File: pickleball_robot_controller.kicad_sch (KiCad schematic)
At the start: 74 parts, among them J1 BATTERY_XT60_PIGTAIL, J10 PI_UART_CONTROL, J11 SERVO_6V_10A_INPUT, J12 MAIN_SWING_25KG_SERVO, J13 ELBOW_MG996R_SERVO, J14 WRIST_MG90S_SERVO, J2 ESP32_PICO_KIT_V4.1_CARRIER, J4 LEFT_MOTOR, J5 RIGHT_MOTOR, J6 LEFT_ENCODER, J7 RIGHT_ENCODER, J8 PI_5V_5A_INPUT, J9 PI_POWER_OUT_2x5V_2xGND, U1 LM2596S-5.0, U2 VNH5019A-E, U3 VNH5019A-E, U5 PCA9685PW, U6 74LVC1G14, U7 74LVC1G14, U8 74LVC1G14, U9 74LVC1G14

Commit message: Improve schematic readability and add power guidance
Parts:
- added D5: GREEN: ESP32/LOGIC, LED_SMD:LED_0805_2012Metric, symbol Device:LED
- added D6: BLUE: PI 5V, LED_SMD:LED_0805_2012Metric, symbol Device:LED
- added D7: AMBER: SERVO 6V, LED_SMD:LED_0805_2012Metric, symbol Device:LED
- added D8: RED: MOTOR FAULT, LED_SMD:LED_0805_2012Metric, symbol Device:LED
- added R100: 1k CTRL POWER, Resistor_SMD:R_0805_2012Metric, symbol Device:R
- added R101: 1k PI POWER, Resistor_SMD:R_0805_2012Metric, symbol Device:R
- added R102: 1k SERVO POWER, Resistor_SMD:R_0805_2012Metric, symbol Device:R
- added R103: 1k FAULT LED, Resistor_SMD:R_0805_2012Metric, symbol Device:R
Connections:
- net +5V_CTRL: now also R100.2
- net 3V3: now also R103.2
- net GND: now also D5.1 (K), D6.1 (K), D7.1 (K)
- net MOTOR_DIAG: now also D8.1 (K)
- net PI_5V: now also R101.2
- net SERVO_6V: now also R102.2
- new net LED_CTRL_PWR: D5.2 (A), R100.1
- new net LED_FAULT_ANODE: D8.2 (A), R103.1
- new net LED_PI_PWR: D6.2 (A), R101.1
- new net LED_SERVO_PWR: D7.2 (A), R102.1
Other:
- note added: "Green = ESP32 logic alive; blue = Pi 5V present; amber = servo 6V present; red = motor driver fault."
- note added: "One 3S battery is used. Separate regulators create PI_5V, +5V_CTRL, and SERVO_6V."
- note added: "STATUS LEDs"
- note added: "Servo 1 = main swing; Servo 2 = elbow; Servo 3 = wrist. Pin order: GND / regulated 6V / PWM."
- note removed: "Servo pin order: 1 GND, 2 regulated 6V, 3 PWM. Verify cable colors before plugging in."

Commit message: Add Pi 5V buck design and clean schematic layout
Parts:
- removed J8: PI_5V_5A_INPUT, TerminalBlock:TerminalBlock_MaiXu_MX126-5.0-02P_1x02_P5.00mm, symbol Connector_Generic:Conn_01x02
- added C31: 100nF BOOT, Capacitor_SMD:C_0805_2012Metric, symbol Device:C
- added C32, C33, C34, C35: 2.2uF 25V X7R, Capacitor_SMD:C_1206_3216Metric, symbol Device:C
- added C36: 4.7nF COMP, Capacitor_SMD:C_0805_2012Metric, symbol Device:C
- added C37: 47pF COMP, Capacitor_SMD:C_0805_2012Metric, symbol Device:C
- added C38, C39, C44: 47uF 10V X7R, Capacitor_SMD:C_1210_3225Metric, symbol Device:C
- added D9: B560C 5A, Diode_SMD:D_SMC, symbol Device:D_Schottky
- added F3: 5A PI OUTPUT FUSE, Fuse:Fuse_1206_3216Metric, symbol Device:Fuse
- added L2: 7.2uH >=8A SHIELDED, Inductor_SMD:L_1210_3225Metric, symbol Device:L
- added R30: 243k RT SET, Resistor_SMD:R_0805_2012Metric, symbol Device:R
- added R31: 442k FB TOP 1%, Resistor_SMD:R_0805_2012Metric, symbol Device:R
- added R32: 90.9k FB BOTTOM 1%, Resistor_SMD:R_0805_2012Metric, symbol Device:R
- added R33: 10.2k COMP, Resistor_SMD:R_0805_2012Metric, symbol Device:R
- added U4: TPS54560BDDA — 5V / 5A, Package_SO:TI_SO-PowerPAD-8_ThermalVias, symbol Regulator_Switching:TPS54560BDDA
- C30: value 1000uF 10V LOW_ESR -> 1000uF 10V LOW ESR
- D5: value GREEN: ESP32/LOGIC -> GREEN
- D6: value BLUE: PI 5V -> BLUE
- D7: value AMBER: SERVO 6V -> AMBER
- D8: value RED: MOTOR FAULT -> RED
- J9: value PI_POWER_OUT_2x5V_2xGND -> PI POWER: 2x5V + 2xGND
- R100: value 1k CTRL POWER -> 1k
- R101: value 1k PI POWER -> 1k
- R102: value 1k SERVO POWER -> 1k
- R103: value 1k FAULT LED -> 1k
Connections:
- net +5V_CTRL: now also R100.1; no longer R100.2
- net 3V3: now also R103.1; no longer R103.2
- net GND: now also D5.2 (A), D6.2 (A), D7.2 (A), C32.2, C33.2, C34.2, C35.2, C36.2, C37.2, C38.2, C39.2, C44.2, D9.1 (K), R30.2, R32.2, U4.7 (GND), U4.9 (GND); no longer D5.1 (K), D6.1 (K), D7.1 (K)
- net LED_CTRL_PWR: now also D5.1 (K), R100.2; no longer D5.2 (A), R100.1
- net LED_FAULT_ANODE: now also D8.1 (K), R103.2; no longer D8.2 (A), R103.1
- net LED_PI_PWR: now also D6.1 (K), R101.2; no longer D6.2 (A), R101.1
- net LED_SERVO_PWR: now also D7.1 (K), R102.2; no longer D7.2 (A), R102.1
- net MOTOR_DIAG: now also D8.2 (A); no longer D8.1 (K)
- net PI_5V: now also R101.1, F3.2; no longer R101.2
- net SERVO_6V: now also R102.1; no longer R102.2
- net VBAT_SW: now also C32.1, C33.1, C34.1, C35.1, U4.2 (VIN), U4.3 (EN)
- new net PI_5V_RAW: C38.1, C39.1, C44.1, F3.1, L2.2, R31.1
- new net PI_BOOT: C31.1, U4.1 (BOOT)
- new net PI_BUCK_SW: C31.2, D9.2 (A), L2.1, U4.8 (SW)
- new net PI_COMP: C37.1, R33.1, U4.6 (COMP)
- new net PI_COMP_RC: C36.1, R33.2
- new net PI_FB: R31.2, R32.1, U4.5 (FB)
- new net PI_RT: R30.1, U4.4 (RT/CLK)
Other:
- note added: "D5 GREEN: control 5V D6 BLUE: Pi 5V D7 AMBER: servo 6V D8 RED: motor driver fault"
- note added: "ESP32-PICO-KIT carrier uses the confirmed 17.78mm row spacing."
- note added: "RASPBERRY PI 5V / 5A BUCK — TPS54560B"
- note added: "U4 values are the TI 12V-to-5V / 5A reference design. Follow TI layout guidance; do not use this rail for motors or servos."
- note added: "Use Mini-Fit Jr / screw terminal, not 0.1in headers, for Pi power. Keep this 5A path short and wide."
- note removed: "DIP-34 W17.78mm is a provisional carrier pad pattern; verify against the real board before ordering."
- note removed: "Green = ESP32 logic alive; blue = Pi 5V present; amber = servo 6V present; red = motor driver fault."
- note removed: "One 3S battery is used. Separate regulators create PI_5V, +5V_CTRL, and SERVO_6V."
- note removed: "RASPBERRY PI 5 POWER PASS-THROUGH (SEPARATE 5V/5A REGULATOR)"
- note removed: "Use Mini-Fit Jr / screw terminal, not ordinary 0.1in headers, for Pi 5 A power."

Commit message: Right-size servo power and add motor cable connectors
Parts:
- removed J4: LEFT_MOTOR, TerminalBlock:TerminalBlock_MaiXu_MX126-5.0-02P_1x02_P5.00mm, symbol Connector_Generic:Conn_01x02
- removed J5: RIGHT_MOTOR, TerminalBlock:TerminalBlock_MaiXu_MX126-5.0-02P_1x02_P5.00mm, symbol Connector_Generic:Conn_01x02
- removed J6: LEFT_ENCODER, Connector_JST:JST_XH_B4B-XH-A_1x04_P2.50mm_Vertical, symbol Connector_Generic:Conn_01x04
- removed J7: RIGHT_ENCODER, Connector_JST:JST_XH_B4B-XH-A_1x04_P2.50mm_Vertical, symbol Connector_Generic:Conn_01x04
- added C45: 100nF BOOT, Capacitor_SMD:C_0805_2012Metric, symbol Device:C
- added C46, C47: 2.2uF 25V X7R, Capacitor_SMD:C_1206_3216Metric, symbol Device:C
- added C48: 4.7nF COMP, Capacitor_SMD:C_0805_2012Metric, symbol Device:C
- added C49: 47pF COMP, Capacitor_SMD:C_0805_2012Metric, symbol Device:C
- added C50, C51: 47uF 10V X7R, Capacitor_SMD:C_1210_3225Metric, symbol Device:C
- added D10: B560C 5A, Diode_SMD:D_SMC, symbol Device:D_Schottky
- added J4: LEFT_GA25_370_MOTOR_ENCODER, Connector_JST:JST_GH_BM06B-GHS-TBT_1x06-1MP_P1.25mm_Vertical, symbol Connector_Generic:Conn_01x06
- added J5: RIGHT_GA25_370_MOTOR_ENCODER, Connector_JST:JST_GH_BM06B-GHS-TBT_1x06-1MP_P1.25mm_Vertical, symbol Connector_Generic:Conn_01x06
- added L3: 6.8uH >=8A SHIELDED, Inductor_SMD:L_1210_3225Metric, symbol Device:L
- added R104: 243k RT SET, Resistor_SMD:R_0805_2012Metric, symbol Device:R
- added R105: 590k FB TOP 1%, Resistor_SMD:R_0805_2012Metric, symbol Device:R
- added R106: 90.9k FB BOTTOM 1%, Resistor_SMD:R_0805_2012Metric, symbol Device:R
- added R107: 10.2k COMP, Resistor_SMD:R_0805_2012Metric, symbol Device:R
- added U10: TPS54560BDDA — 6V / 5A, Package_SO:TI_SO-PowerPAD-8_ThermalVias, symbol Regulator_Switching:TPS54560BDDA
- F2: value 15A_EXTERNAL_SERVO_FUSE -> 7.5A_SERVO_OUTPUT_FUSE
- J11: value SERVO_6V_10A_INPUT -> SERVO_6V_POWER_OUT
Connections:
- net 3V3: now also J4.4 (Pin_4), J5.4 (Pin_4)
- net GND: now also C46.2, C47.2, C48.2, C49.2, C50.2, C51.2, D10.1 (K), J4.3 (Pin_3), J5.3 (Pin_3), R104.2, R106.2, U10.7 (GND), U10.9 (GND)
- net LEFT_ENC_A_RAW: now also J4.5 (Pin_5)
- net LEFT_ENC_B_RAW: now also J4.6 (Pin_6)
- net LEFT_OUTA: now also J4.1 (Pin_1)
- net LEFT_OUTB: now also J4.2 (Pin_2)
- net RIGHT_ENC_A_RAW: now also J5.5 (Pin_5)
- net RIGHT_ENC_B_RAW: now also J5.6 (Pin_6)
- net RIGHT_OUTA: now also J5.1 (Pin_1)
- net RIGHT_OUTB: now also J5.2 (Pin_2)
- net SERVO_6V: now also J11.1 (Pin_1)
- net SERVO_6V_RAW: now also C50.1, C51.1, L3.2, R105.1; no longer J11.1 (Pin_1)
- net VBAT_SW: now also C46.1, C47.1, U10.2 (VIN), U10.3 (EN)
- new net SERVO_BOOT: C45.1, U10.1 (BOOT)
- new net SERVO_BUCK_SW: C45.2, D10.2 (A), L3.1, U10.8 (SW)
- new net SERVO_COMP: C49.1, R107.1, U10.6 (COMP)
- new net SERVO_COMP_RC: C48.1, R107.2
- new net SERVO_FB: R105.2, R106.1, U10.5 (FB)
- new net SERVO_RT: R104.1, U10.4 (RT/CLK)
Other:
- note added: "Five amp rail is deliberate: enough for normal 3-servo operation, with the 7.5A fuse limiting the branch."
- note added: "J4/J5 are six-pin JST-GH 1.25mm: motor+/motor-/GND/+3V3/encoder-A/encoder-B."
- note added: "SERVO 6V / 5A BUCK — TPS54560B"
- note added: "WHEEL ENCODERS — BUILT INTO J4/J5 (3.3V)"
- note removed: "WHEEL ENCODERS (3.3V)"

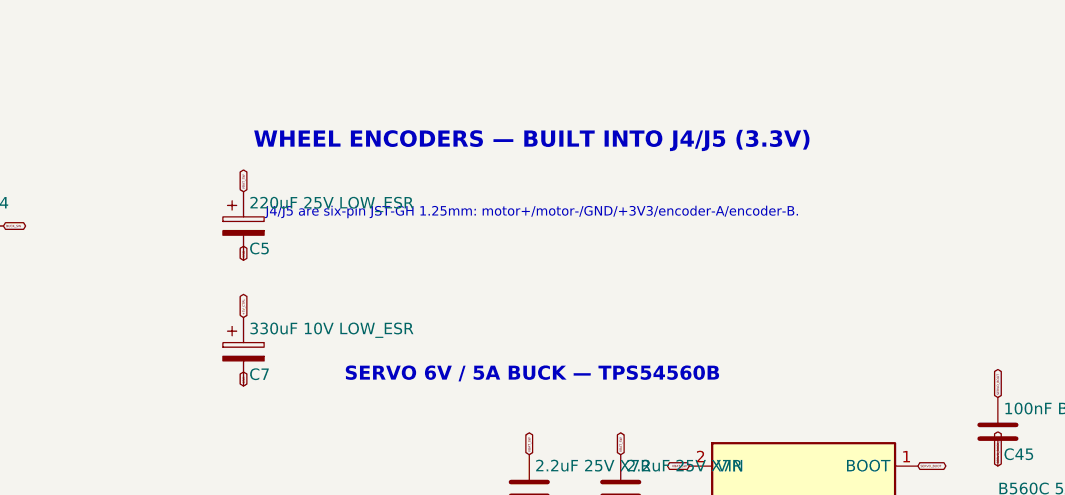
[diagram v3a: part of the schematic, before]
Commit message: Correct GA25 motor connector to JST PH 2mm
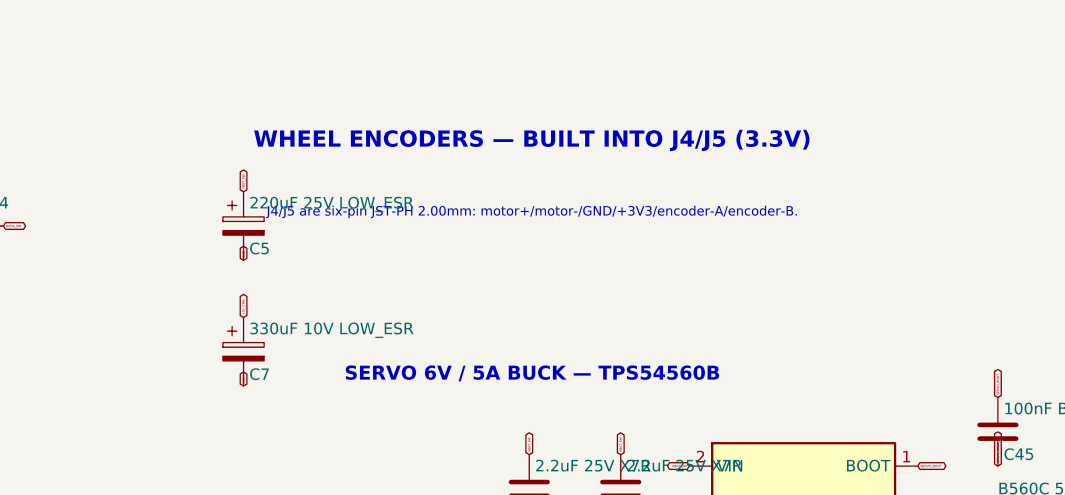
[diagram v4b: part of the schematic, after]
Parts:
- J4, J5: footprint Connector_JST:JST_GH_BM06B-GHS-TBT_1x06-1MP_P1.25mm_Vertical -> Connector_JST:JST_PH_B6B-PH-K_1x06_P2.00mm_Vertical
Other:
- note added: "J4/J5 are six-pin JST-PH 2.00mm: motor+/motor-/GND/+3V3/encoder-A/encoder-B."
- note removed: "J4/J5 are six-pin JST-GH 1.25mm: motor+/motor-/GND/+3V3/encoder-A/encoder-B."

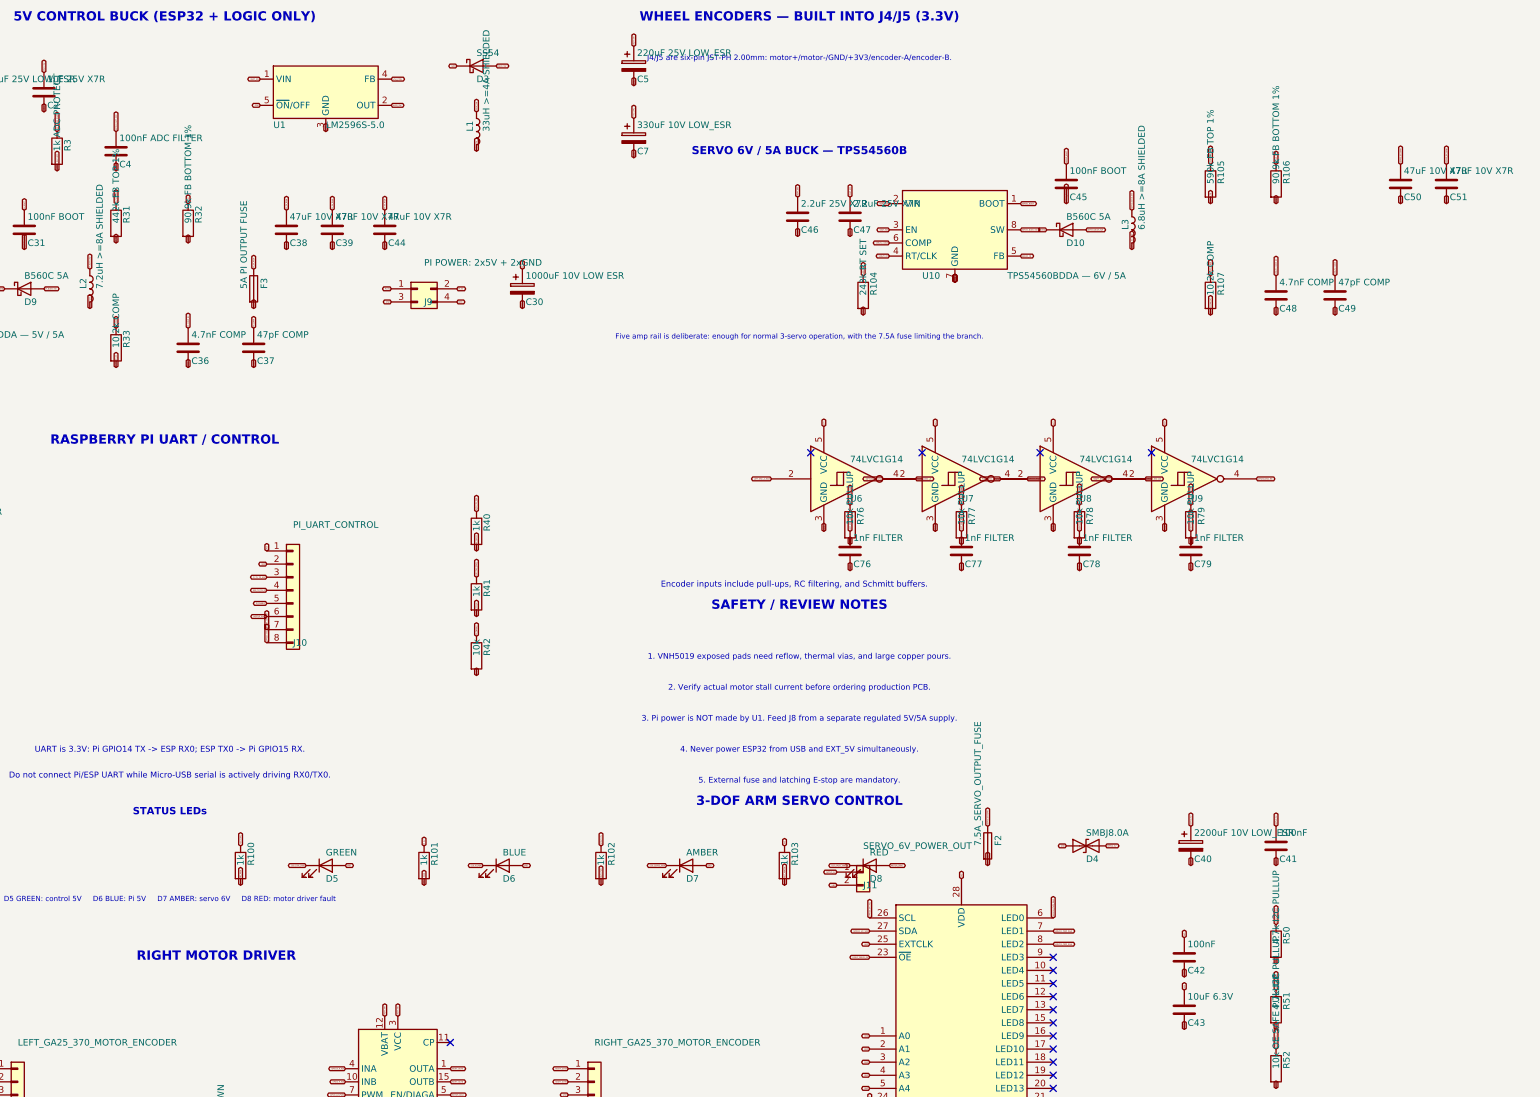
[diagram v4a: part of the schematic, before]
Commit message: Use standard servo headers and solderable power parts
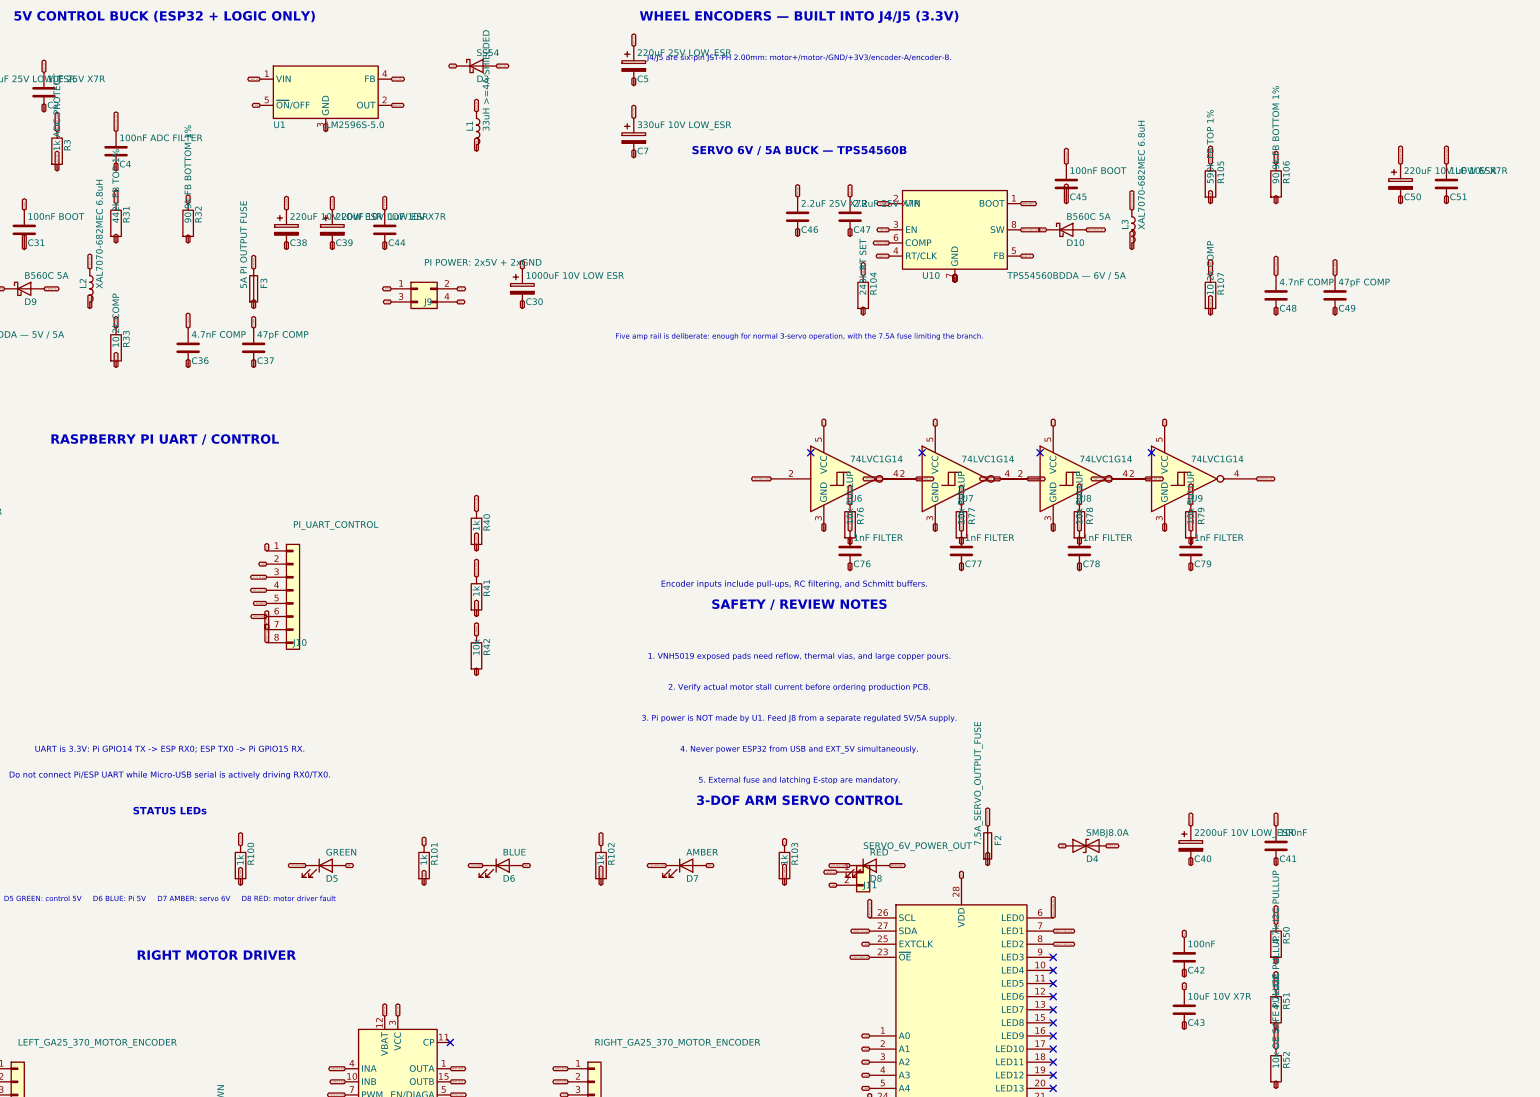
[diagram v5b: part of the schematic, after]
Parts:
- removed C38, C39, C50: 47uF 10V X7R, Capacitor_SMD:C_1210_3225Metric, symbol Device:C
- added C38, C39, C50: 220uF 10V LOW ESR, Capacitor_THT:CP_Radial_D8.0mm_P3.50mm, symbol Device:C_Polarized
- C2, C32, C33, C34, C35, C46, C47: footprint Capacitor_SMD:C_1206_3216Metric -> Capacitor_SMD:C_0805_2012Metric
- C43: value 10uF 6.3V -> 10uF 10V X7R; footprint Capacitor_SMD:C_1206_3216Metric -> Capacitor_SMD:C_0805_2012Metric
- C44, C51: value 47uF 10V X7R -> 1uF 10V X7R; footprint Capacitor_SMD:C_1210_3225Metric -> Capacitor_SMD:C_0805_2012Metric
- J12, J13, J14: footprint Connector_JST:JST_XH_B3B-XH-A_1x03_P2.50mm_Vertical -> Connector_PinHeader_2.54mm:PinHeader_1x03_P2.54mm_Vertical
- L2: value 7.2uH >=8A SHIELDED -> XAL7070-682MEC 6.8uH; footprint Inductor_SMD:L_1210_3225Metric -> Inductor_SMD:L_Coilcraft_XAL7070-XXX
- L3: value 6.8uH >=8A SHIELDED -> XAL7070-682MEC 6.8uH; footprint Inductor_SMD:L_1210_3225Metric -> Inductor_SMD:L_Coilcraft_XAL7070-XXX
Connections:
- net GND: now also C38.2, C39.2, C50.2
- net PI_5V_RAW: now also C38.1, C39.1
- net SERVO_6V_RAW: now also C50.1
